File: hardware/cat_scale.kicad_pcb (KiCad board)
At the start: 2 copper layers, 72.5 x 35.5 mm, 40 parts, among them J1 USB_C_Receptacle_USB2.0, J2 UART, J3 I2C, J4 LOAD CELL, J5 SSD1306, Q1 S8550, SW1 RST, SW2 BOOT, SW3 RotaryEncoder_Switch, U1 ESP32-S2-SOLO-U, U2 AMS1117-3.3, U3 HX711

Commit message: Fixed PCB design
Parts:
- removed Q1: S8550, Package_TO_SOT_SMD:SOT-23
- added J6: Conn_01x02_Pin, Connector_PinHeader_2.54mm:PinHeader_1x02_P2.54mm_Vertical, B.Cu at (139.2, 99.1)
- added Q2: MMBT3906, Package_TO_SOT_SMD:SOT-23, B.Cu at (155.4, 105.7)
- added R11: 10k, Resistor_SMD:R_1206_3216Metric, B.Cu at (150.9, 88.4)
- added R12: 10k, Resistor_SMD:R_1206_3216Metric, B.Cu at (153.4, 88.4)
- C8: value 1uF -> 10uF
- C9: value 1uF -> 0.1uF
- D1: value POWER -> PWR
- U1: value ESP32-S2-SOLO-U -> ESP32-S2-SOLO-U-N4R2
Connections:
- C5 pad 2: Net-(D2-K) -> +5V
- D2 pad 1: Net-(D2-K) -> +5V
- J3 pad 3: /SDA -> /SCL
- J3 pad 4: /SCL -> /SDA
- J5 pad 1: +3V3 -> +5V
- J5 pad 3: /SDA -> /SCL
- J5 pad 4: /SCL -> /SDA
- U1 pad 24: /SCL -> unconnected-(U1-IO33-Pad24)
- U1 pad 25: /SDA -> unconnected-(U1-IO34-Pad25)
- U1 pad 34: unconnected-(U1-IO41-Pad34) -> /SCL
- U1 pad 35: unconnected-(U1-IO42-Pad35) -> /SDA
- U2 pad 3: Net-(D2-K) -> +5V
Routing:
- net +5V: track 0.00 -> 22.5 mm
- net /SDA: track 27.7 -> 12.2 mm
- net /SCL: track 26.3 -> 13.6 mm
- net Net-(D2-A): track 10.4 -> 17.4 mm
- net Net-(D2-K): track 5.76 -> 0.00 mm
- net Net-(J1-D--PadA7): track 3.07 -> 6.33 mm
- net /AVDD: track 38.2 -> 40.9 mm
- net Net-(Q2-B): track 13.3 -> 15.5 mm
- net /ROT1: track 5.82 -> 7.24 mm
- net GND: track 0.00 -> 1.38 mm, vias 9 -> 8
- net +3V3: track 153.3 -> 154.2 mm, vias 4 -> 5
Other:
- board text added: "3V3"
- board text added: "5V"
- board text added: "A+"
- board text added: "A-"
- board text added: "GND"
- board text added: "RXD"
- board text added: "SCL"
- board text added: "SDA"
- board text added: "TXD"
- board text added: "VDD"
- board text added: "WeightWhiskers v0.2"
- board text added: "https://github.com/fehlfarbe/weight-whiskers"
- board text removed: "WeightWhiskers v0.1"

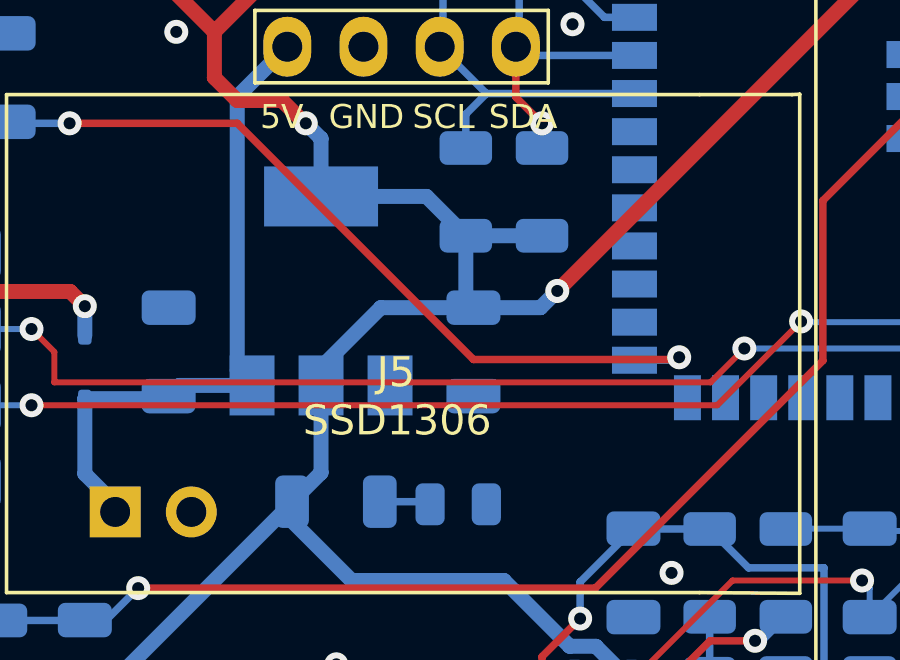
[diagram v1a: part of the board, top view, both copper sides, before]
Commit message: * PCB: Added buzzer
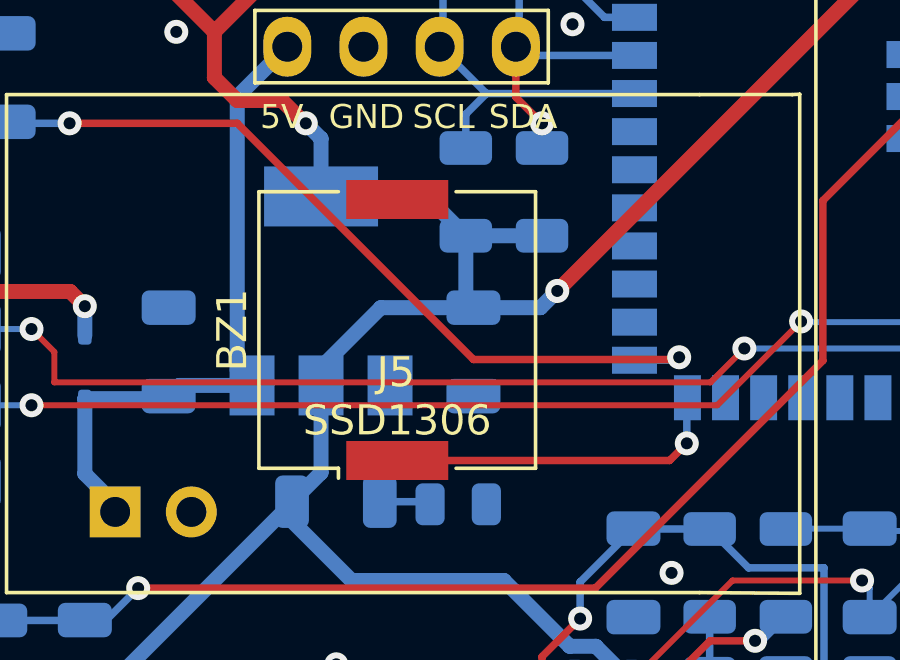
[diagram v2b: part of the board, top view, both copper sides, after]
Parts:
- added BZ1: Buzzer, Buzzer_Beeper:Buzzer_Murata_PKMCS0909E, F.Cu at (148.6, 93.0)
- Q2: value MMBT3906 -> MMBT4403
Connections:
- U1 pad 26: unconnected-(U1-IO45-Pad26) -> /BUZZ
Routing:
- net /BUZZ: track 0.00 -> 11.4 mm, vias 0 -> 1

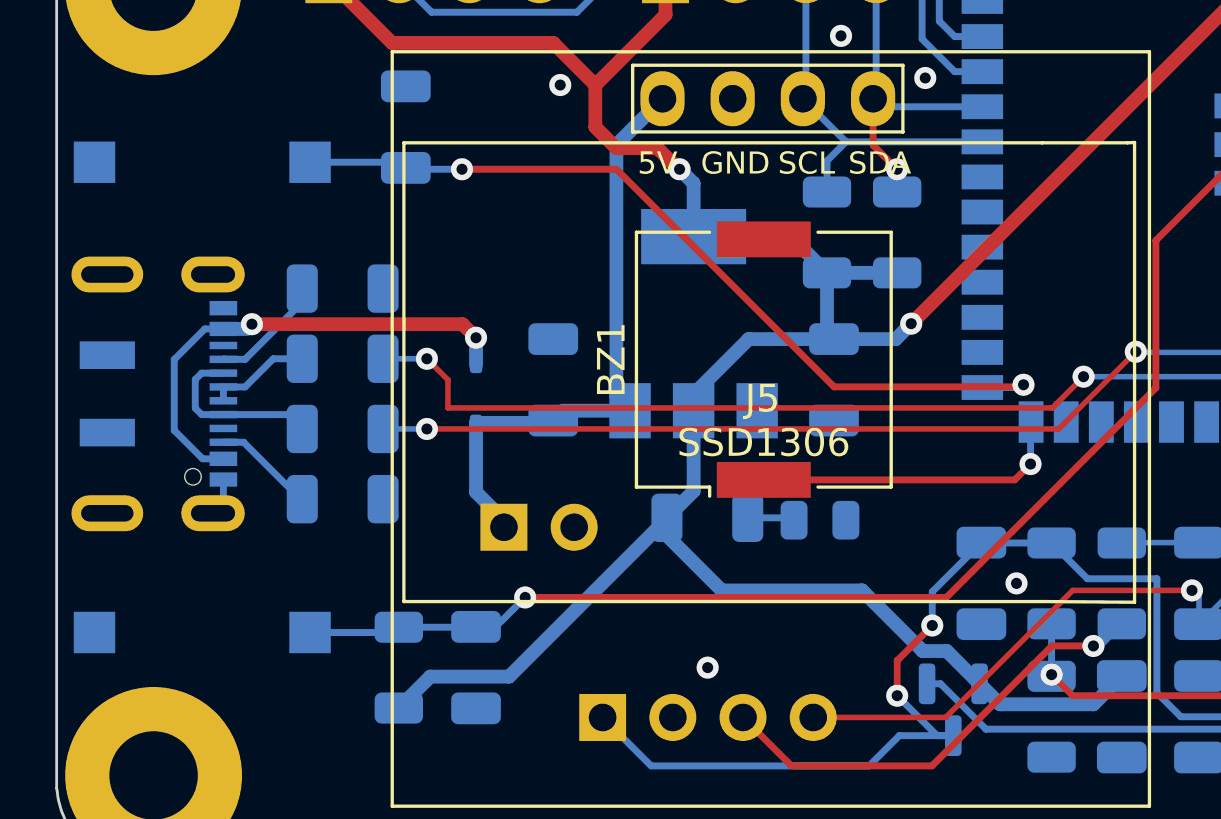
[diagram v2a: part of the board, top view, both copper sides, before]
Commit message: Updated PCB and added images of the PCB to README
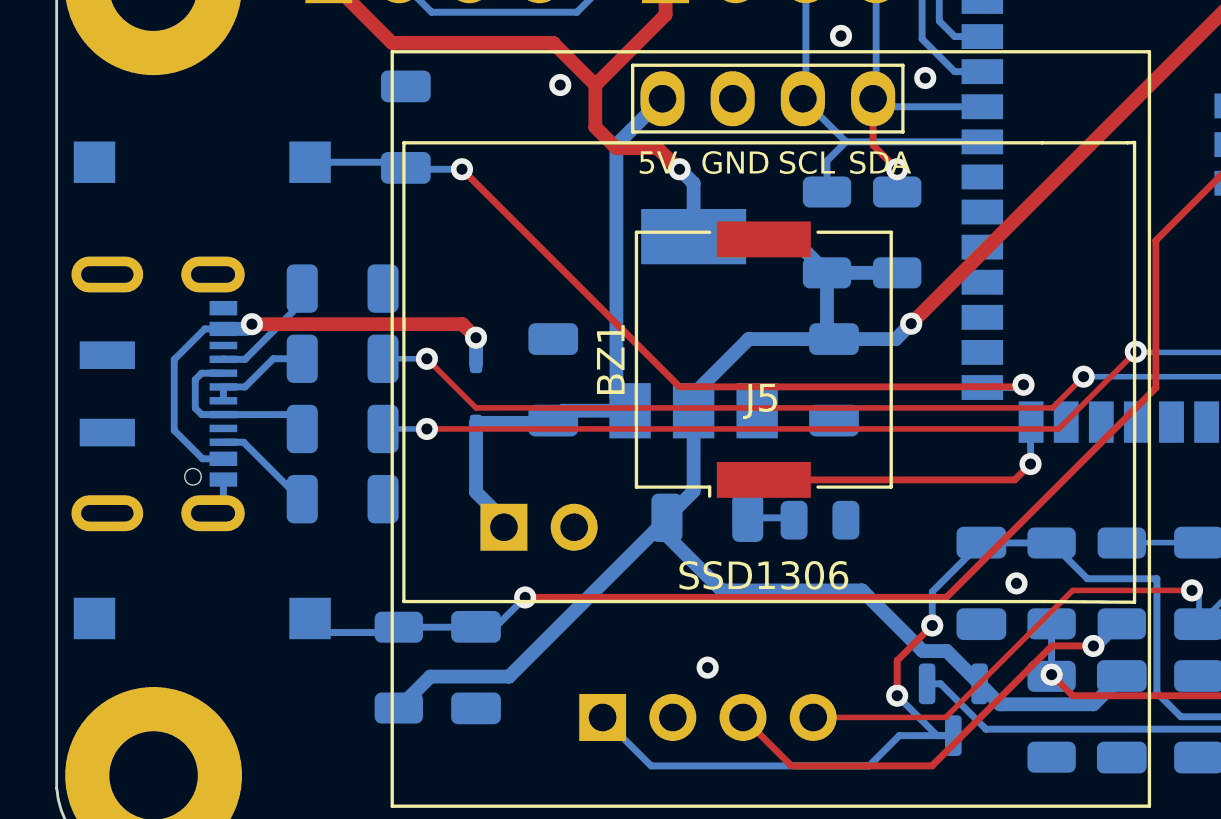
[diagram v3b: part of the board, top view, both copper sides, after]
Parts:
- moved SW1 0.51 mm to (128.3, 102.4)
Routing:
- net /USB_D+: track 41.1 -> 40.6 mm
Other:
- board text added: "WeightWhiskers v0.3"
- board text removed: "WeightWhiskers v0.2"
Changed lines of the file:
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@@
       (sketchpadsonfab false)
       (subtractmaskfromsilk false)
-      (outputformat 5)
+      (outputformat 1)
       (mirror false)
       (drillshape 0)
       (scaleselection 1)
-      (outputdirectory "stencil")
+      (outputdirectory "gerbers")
     )
   )
@@
         (effects (font (size 1 1) (thickness 0.15)))
     )
-    (fp_text value "SSD1306" (at 0.046 1.858) (layer "F.SilkS")
+    (fp_text value "SSD1306" (at 0.046 6.684) (layer "F.SilkS")
         (effects (font (size 1 1) (thickness 0.15)))
     )
@@
     (fp_line (start 1.6 0.8) (end 1.6 -0.8)
       (stroke (width 0.1) (type solid)) (layer "B.Fab"))
-    (pad "1" smd roundrect (at -1.4625 0 270) (size 1.125 1.75) (layers "B.Cu" "B.Paste" "B.Mask") (roundrect_rratio 0.222222)
+    (pad "1" smd roundrect (at -1.4625 0 270) (size 1.125 1.75) (layers "B.Cu" "B.Paste" "B.Mask") (roundrect_rratio 0.2222222222)
       (net 21 "/SCL") (pintype "passive"))
-    (pad "2" smd roundrect (at 1.4625 0 270) (size 1.125 1.75) (layers "B.Cu" "B.Paste" "B.Mask") (roundrect_rratio 0.222222)
+    (pad "2" smd roundrect (at 1.4625 0 270) (size 1.125 1.75) (layers "B.Cu" "B.Paste" "B.Mask") (roundrect_rratio 0.2222222222)
       (net 4 "+3V3") (pintype "passive"))
     (model "${KICAD6_3DMODEL_DIR}/Resistor_SMD.3dshapes/R_1206_3216Metric.wrl"
@@
   )
   (footprint "Button_Switch_SMD:SW_SPST_CK_RS282G05A3" (layer "B.Cu")
-    (at 128.27 102.87)
+    (at 128.27 102.362)
     (descr "https://www.mouser.com/ds/2/60/RS-282G05A-SM_RT-1159762.pdf")
     (tags "SPST button tactile switch")
@@
     (fp_line (start 1.6 0.8) (end 1.6 -0.8)
       (stroke (width 0.1) (type solid)) (layer "B.Fab"))
-    (pad "1" smd roundrect (at -1.4625 0 270) (size 1.125 1.75) (layers "B.Cu" "B.Paste" "B.Mask") (roundrect_rratio 0.222222)
+    (pad "1" smd roundrect (at -1.4625 0 270) (size 1.125 1.75) (layers "B.Cu" "B.Paste" "B.Mask") (roundrect_rratio 0.2222222222)
       (net 22 "/SDA") (pintype "passive"))
-    (pad "2" smd roundrect (at 1.4625 0 270) (size 1.125 1.75) (layers "B.Cu" "B.Paste" "B.Mask") (roundrect_rratio 0.222222)
+    (pad "2" smd roundrect (at 1.4625 0 270) (size 1.125 1.75) (layers "B.Cu" "B.Paste" "B.Mask") (roundrect_rratio 0.2222222222)
       (net 4 "+3V3") (pintype "passive"))
     (model "${KICAD6_3DMODEL_DIR}/Resistor_SMD.3dshapes/R_1206_3216Metric.wrl"
@@
     (effects (font (size 0.8 0.8) (thickness 0.15)) (justify left bottom mirror))
   )
-  (gr_text "WeightWhiskers v0.2" (at 189.23 85.09 90) (layer "B.SilkS")
+  (gr_text "WeightWhiskers v0.3" (at 189.23 85.09 90) (layer "B.SilkS")
     (effects (font (size 1.2 1.2) (thickness 0.2) bold) (justify left bottom mirror))
   )
@@
   (segment (start 129.034 97.334) (end 129.034 98.179) (width 0.25) (layer "B.Cu") (net 1))
   (segment (start 129.034 98.179) (end 128.659 98.554) (width 0.25) (layer "B.Cu") (net 1))
-  (segment (start 143.256 86.106) (end 137.668 86.106) (width 0.25) (layer "F.Cu") (net 2))
-  (segment (start 157.912498 93.98) (end 151.13 93.98) (width 0.25) (layer "F.Cu") (net 2))
-  (segment (start 157.988 93.904498) (end 157.912498 93.98) (width 0.25) (layer "F.Cu") (net 2))
-  (segment (start 151.13 93.98) (end 143.256 86.106) (width 0.25) (layer "F.Cu") (net 2))
+  (segment (start 157.912498 93.98) (end 157.988 93.904498) (width 0.25) (layer "F.Cu") (net 2))
+  (segment (start 145.542 93.98) (end 157.912498 93.98) (width 0.25) (layer "F.Cu") (net 2))
+  (segment (start 137.668 86.106) (end 145.542 93.98) (width 0.25) (layer "F.Cu") (net 2))
   (via (at 157.988 93.904498) (size 0.8) (drill 0.4) (layers "F.Cu" "B.Cu") (net 2))
   (via (at 137.668 86.106) (size 0.8) (drill 0.4) (layers "F.Cu" "B.Cu") (net 2))
@@
   (segment (start 173.998 92.734) (end 162.076 92.734) (width 0.2) (layer "B.Cu") (net 25))
   (segment (start 134.8125 95.504) (end 136.398 95.504) (width 0.2) (layer "B.Cu") (net 25))
-  (segment (start 136.398 92.964) (end 137.16 93.726) (width 0.2) (layer "F.Cu") (net 26))
   (segment (start 159.030756 94.742) (end 160.160378 93.612378) (width 0.2) (layer "F.Cu") (net 26))
-  (segment (start 137.16 94.742) (end 159.030756 94.742) (width 0.2) (layer "F.Cu") (net 26))
-  (segment (start 137.16 93.726) (end 137.16 94.742) (width 0.2) (layer "F.Cu") (net 26))
+  (segment (start 138.176 94.742) (end 136.398 92.964) (width 0.2) (layer "F.Cu") (net 26))
+  (segment (start 159.030756 94.742) (end 138.176 94.742) (width 0.2) (layer "F.Cu") (net 26))
   (via (at 160.160378 93.612378) (size 0.8) (drill 0.4) (layers "F.Cu" "B.Cu") (net 26))
   (via (at 136.398 92.964) (size 0.8) (drill 0.4) (layers "F.Cu" "B.Cu") (net 26))

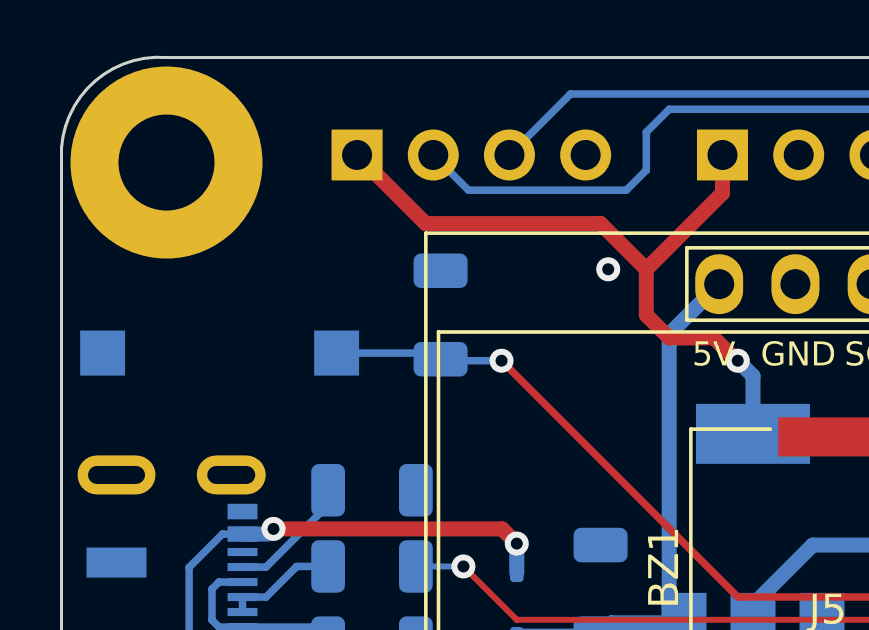
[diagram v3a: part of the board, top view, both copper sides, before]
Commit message: Updated PCB and README
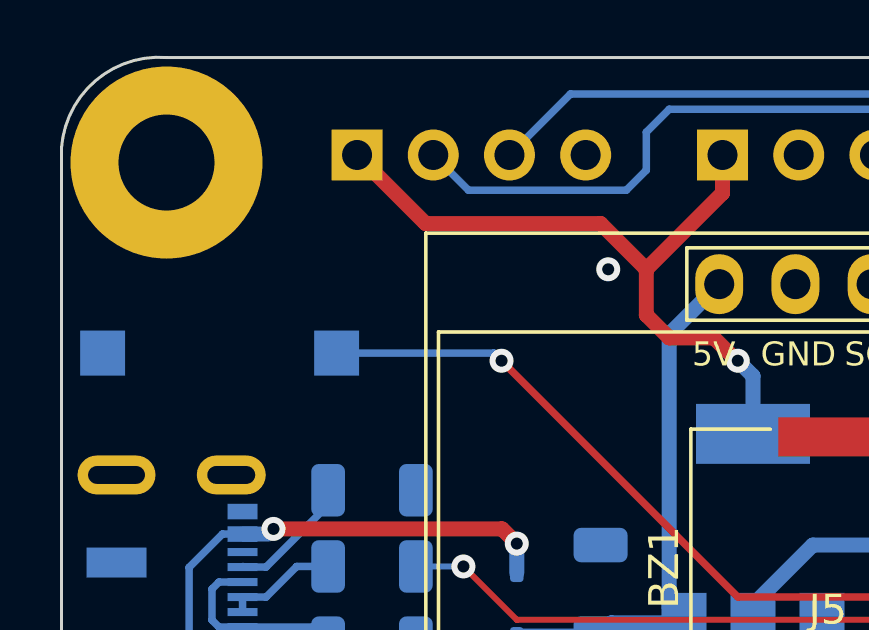
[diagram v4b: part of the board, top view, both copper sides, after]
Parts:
- removed C1: 1uF, Capacitor_SMD:C_1206_3216Metric
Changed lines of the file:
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@@
     )
   )
-  (footprint "Capacitor_SMD:C_1206_3216Metric" (layer "B.Cu")
-    (at 135.636 84.582 -90)
-    (descr "Capacitor SMD 1206 (3216 Metric), square (rectangular) end terminal, IPC_7351 nominal, (Body size source: IPC-SM-782 page 76, https://www.pcb-3d.com/wordpress/wp-content/uploads/ipc-sm-782a_amendment_1_and_2.pdf), generated with kicad-footprint-generator")
-    (tags "capacitor")
-    (property "Sheetfile" "cat_scale.kicad_sch")
-    (property "Sheetname" "")
-    (property "ki_description" "Unpolarized capacitor, small symbol")
-    (property "ki_keywords" "capacitor cap")
-    (attr smd)
-    (fp_text reference "C1" (at 0 -2.032 90) (layer "B.SilkS")
-        (effects (font (size 1 1) (thickness 0.15)) (justify mirror))
-    )
-    (fp_text value "1uF" (at 0 -1.85 90) (layer "B.Fab")
-        (effects (font (size 1 1) (thickness 0.15)) (justify mirror))
-    )
-    (fp_text user "${REFERENCE}" (at 0 0 90) (layer "B.Fab")
-        (effects (font (size 0.8 0.8) (thickness 0.12)) (justify mirror))
-    )
-    (fp_line (start -0.711252 -0.91) (end 0.711252 -0.91)
-      (stroke (width 0.12) (type solid)) (layer "B.SilkS"))
-    (fp_line (start -0.711252 0.91) (end 0.711252 0.91)
-      (stroke (width 0.12) (type solid)) (layer "B.SilkS"))
-    (fp_line (start -2.3 -1.15) (end -2.3 1.15)
-      (stroke (width 0.05) (type solid)) (layer "B.CrtYd"))
-    (fp_line (start -2.3 1.15) (end 2.3 1.15)
-      (stroke (width 0.05) (type solid)) (layer "B.CrtYd"))
-    (fp_line (start 2.3 -1.15) (end -2.3 -1.15)
-      (stroke (width 0.05) (type solid)) (layer "B.CrtYd"))
-    (fp_line (start 2.3 1.15) (end 2.3 -1.15)
-      (stroke (width 0.05) (type solid)) (layer "B.CrtYd"))
-    (fp_line (start -1.6 -0.8) (end -1.6 0.8)
-      (stroke (width 0.1) (type solid)) (layer "B.Fab"))
-    (fp_line (start -1.6 0.8) (end 1.6 0.8)
-      (stroke (width 0.1) (type solid)) (layer "B.Fab"))
-    (fp_line (start 1.6 -0.8) (end -1.6 -0.8)
-      (stroke (width 0.1) (type solid)) (layer "B.Fab"))
-    (fp_line (start 1.6 0.8) (end 1.6 -0.8)
-      (stroke (width 0.1) (type solid)) (layer "B.Fab"))
-    (pad "1" smd roundrect (at -1.475 0 270) (size 1.15 1.8) (layers "B.Cu" "B.Paste" "B.Mask") (roundrect_rratio 0.2173913043)
-      (net 1 "GND") (pintype "passive"))
-    (pad "2" smd roundrect (at 1.475 0 270) (size 1.15 1.8) (layers "B.Cu" "B.Paste" "B.Mask") (roundrect_rratio 0.2173913043)
-      (net 2 "/BOOT") (pintype "passive"))
-    (model "${KICAD6_3DMODEL_DIR}/Capacitor_SMD.3dshapes/C_1206_3216Metric.wrl"
-      (offset (xyz 0 0 0))
-      (scale (xyz 1 1 1))
-      (rotate (xyz 0 0 0))
-    )
-  )
   (footprint "Connector_PinHeader_2.54mm:PinHeader_1x04_P2.54mm_Vertical" (layer "B.Cu")
     (at 132.852 79.248 -90)
@@
   (via (at 137.668 86.106) (size 0.8) (drill 0.4) (layers "F.Cu" "B.Cu") (net 2))
   (segment (start 157.888498 94.004) (end 157.988 93.904498) (width 0.25) (layer "B.Cu") (net 2))
-  (segment (start 135.685 86.106) (end 135.636 86.057) (width 0.25) (layer "B.Cu") (net 2))
-  (segment (start 135.636 86.057) (end 135.431 85.852) (width 0.25) (layer "B.Cu") (net 2))
   (segment (start 156.498 94.004) (end 157.888498 94.004) (width 0.25) (layer "B.Cu") (net 2))
-  (segment (start 137.668 86.106) (end 135.685 86.106) (width 0.25) (layer "B.Cu") (net 2))
-  (segment (start 135.431 85.852) (end 132.17 85.852) (width 0.25) (layer "B.Cu") (net 2))
+  (segment (start 137.414 85.852) (end 132.17 85.852) (width 0.25) (layer "B.Cu") (net 2))
+  (segment (start 137.668 86.106) (end 137.414 85.852) (width 0.25) (layer "B.Cu") (net 2))
   (segment (start 162.777 88.683) (end 162.777 94.017) (width 0.25) (layer "F.Cu") (net 3))
   (segment (start 162.777 94.017) (end 155.194 101.6) (width 0.25) (layer "F.Cu") (net 3))
